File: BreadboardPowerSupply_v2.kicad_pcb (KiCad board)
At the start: 2 copper layers, 30.1 x 52.2 mm, 19 parts, among them J1 Barrel_Jack_Switch, J2 Conn_02x02_Odd_Even, J3 Conn_02x02_Odd_Even, SW1 SW_DPDT_x2, U1 LM7805_TO220

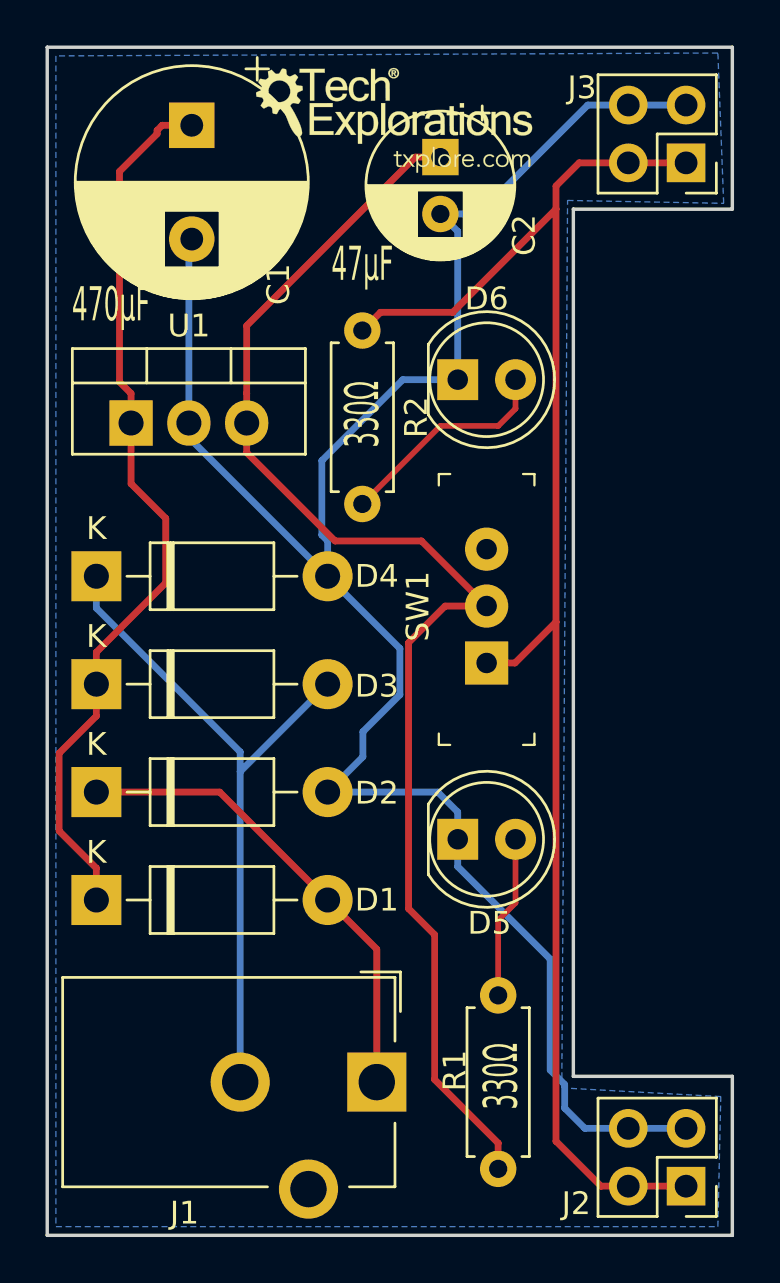
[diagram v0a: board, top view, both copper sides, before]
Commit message: Fixed various cosmetic issues with layout.
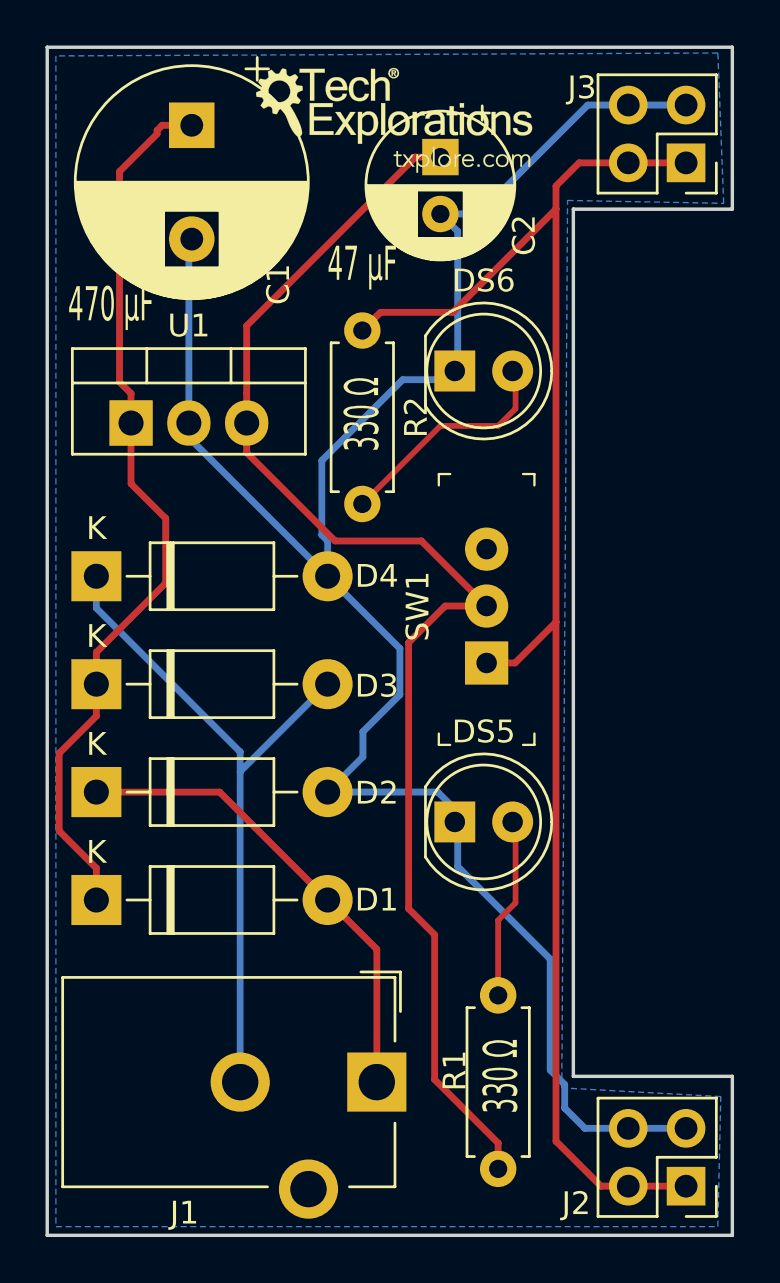
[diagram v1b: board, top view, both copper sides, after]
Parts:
- removed D5, D6: LED, LED_THT:LED_D5.0mm
- added DS5: LED, LED_THT:LED_D5.0mm, F.Cu at (54.9, 141.2)
- added DS6: LED, LED_THT:LED_D5.0mm, F.Cu at (54.9, 121.4)
- C1, C2: value CP1 -> CP
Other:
- board text added: "330 Ω"
- board text added: "47 μF"
- board text added: "470 μF"
- board text removed: "330Ω"
- board text removed: "470μF"
- board text removed: "47μF"
